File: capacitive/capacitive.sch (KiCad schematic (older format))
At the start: 53 parts, among them J101 I2C, J102 UART, J103 SWD, U101 STM32F070C6T6, U102 TLV9062IDR

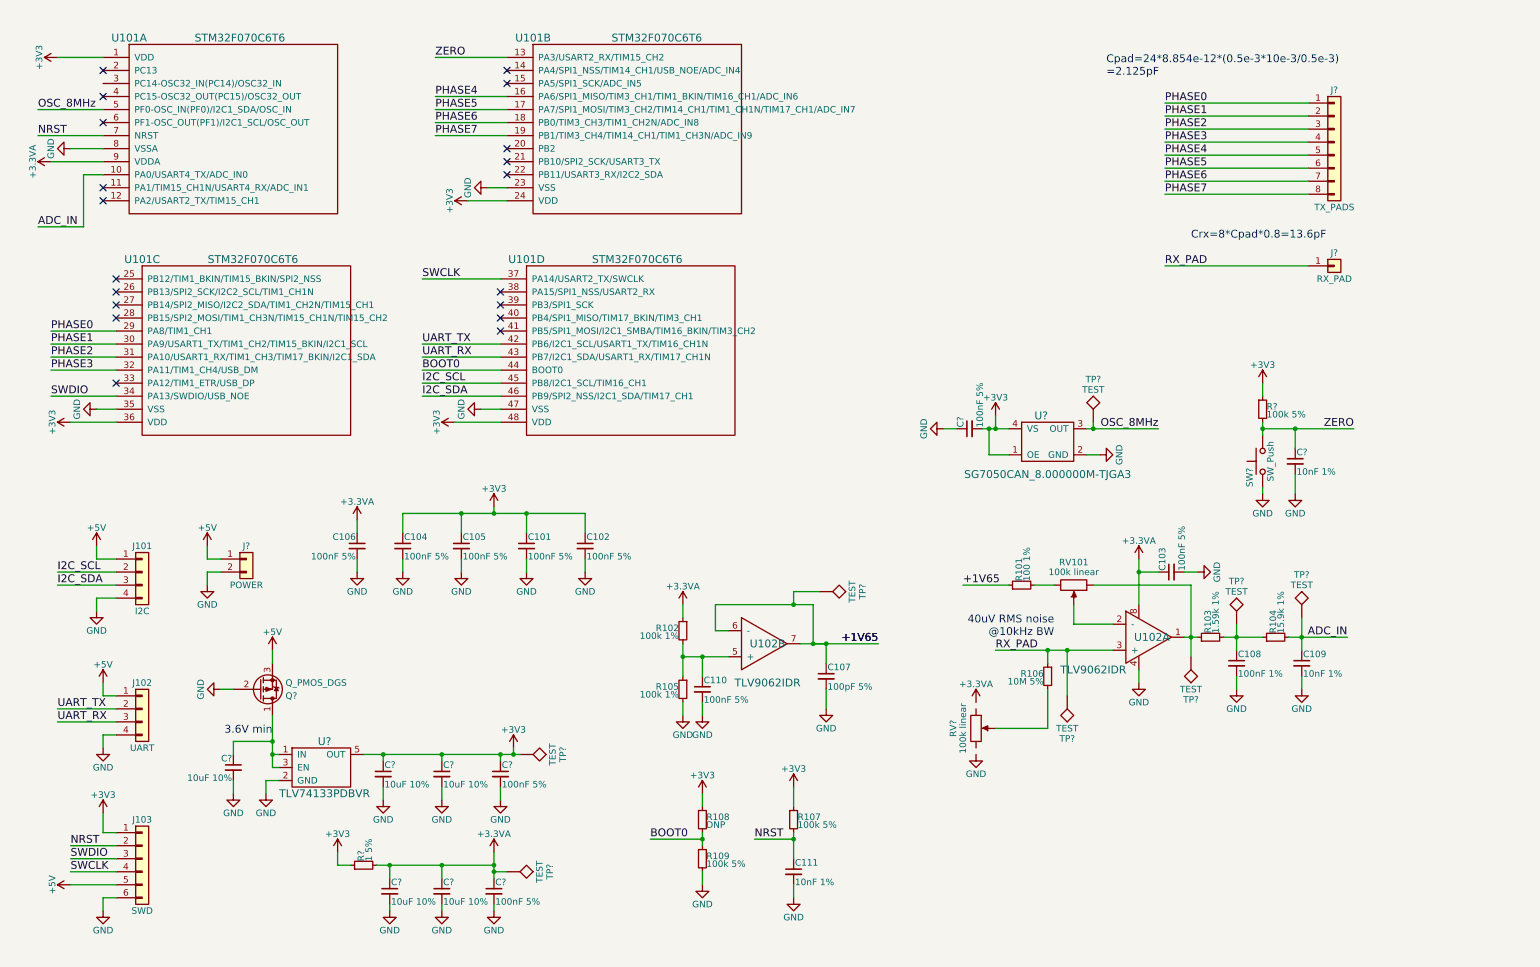
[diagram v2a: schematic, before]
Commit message: Write script to autofill components; save before test
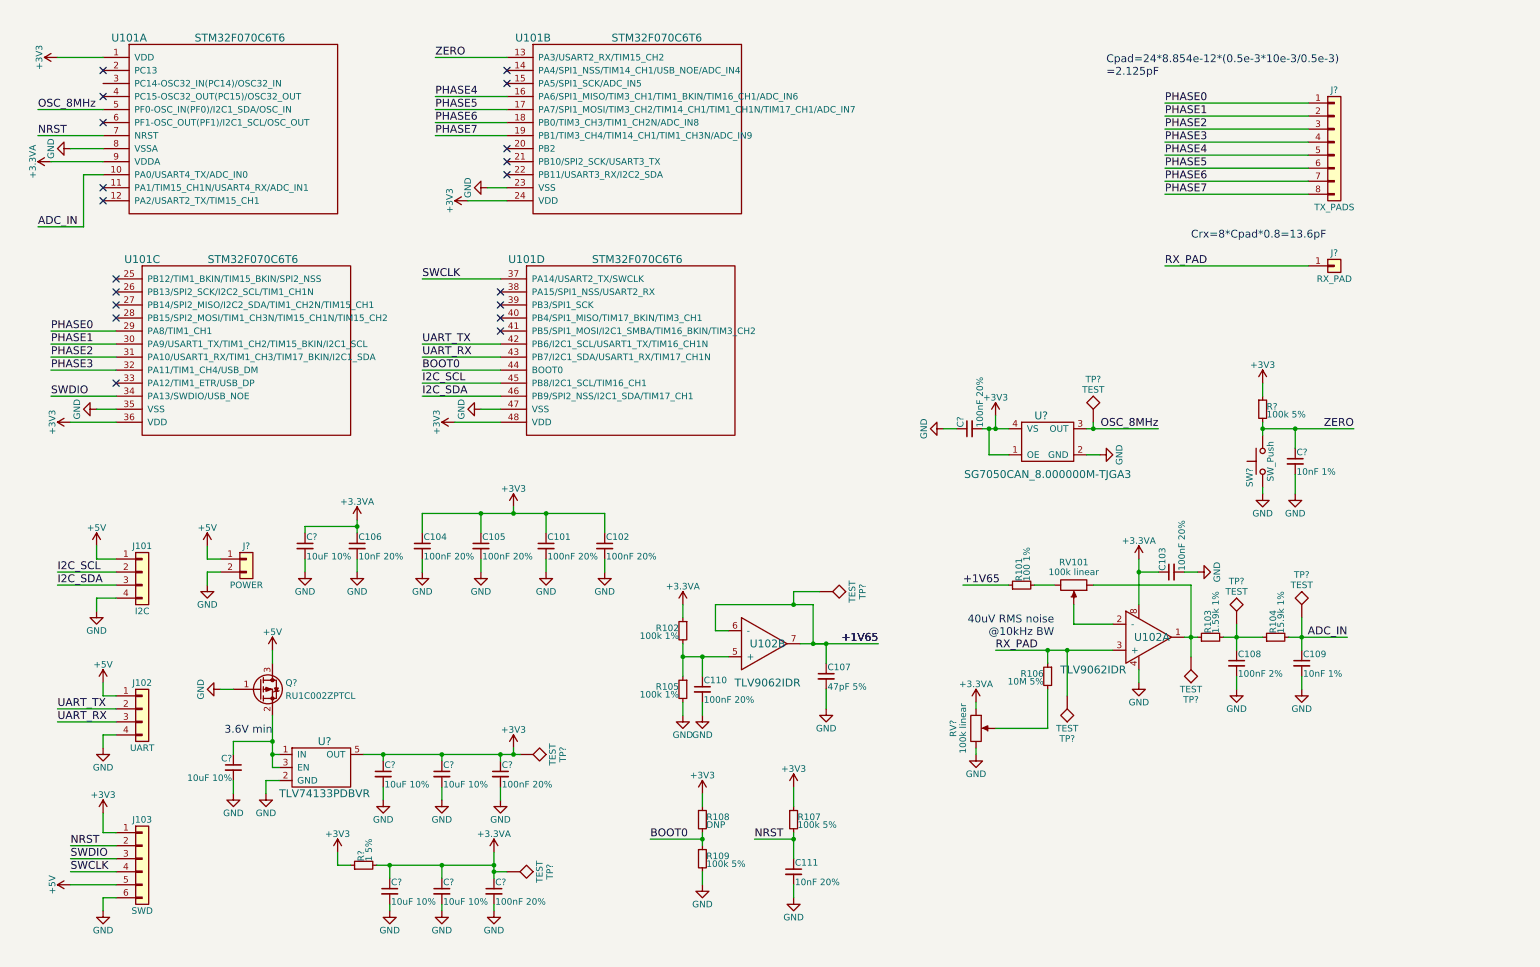
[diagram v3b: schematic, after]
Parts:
- removed Q?: Q_PMOS_DGS, symbol Q_PMOS_DGS
- added C?: 10uF 10%, Capacitors_SMD:C_1210_HandSoldering, symbol C_Small
- added Q?: RU1C002ZPTCL, symbol Q_PMOS_GSD
- C101, C102, C103, C105, C110, C? (x3): value 100nF 5% -> 100nF 20%
- C104: value 100nF 5% -> 100nF 20%; footprint (none) -> Capacitors_SMD:C_0805_HandSoldering; Mouser (none) -> 710-885012207016
- C106: value 100nF 5% -> 10nF 20%
- C107: value 100pF 5% -> 47pF 5%
- C108: value 100nF 1% -> 100nF 2%
- C111: value 10nF 1% -> 10nF 20%
- U101: Mouser (none) -> 511-STM32F070C6T6
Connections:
- net +3.3VA: now also RV?.1, C?.1
- net +5V: now also Q?.3 (D)
- net GND: now also RV?.3, C?.2, Q?.1 (G)
- net at C?.1, U?.1 (IN), U?.3 (EN): now also Q?.2 (S)
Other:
- moved on the sheet: C101, C102, C104, C105
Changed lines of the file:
@@
 L +3V3 #PWR110
 U 1 1 5AFFB346
-P 4250 4350
-F 0 "#PWR110" H 4250 4200 50  0001 C CNN
-F 1 "+3V3" H 4250 4490 50  0000 C CNN
-F 2 "" H 4250 4350 50  0001 C CNN
-F 3 "" H 4250 4350 50  0001 C CNN
-	1    4250 4350
+P 4400 4350
+F 0 "#PWR110" H 4400 4200 50  0001 C CNN
+F 1 "+3V3" H 4400 4490 50  0000 C CNN
+F 2 "" H 4400 4350 50  0001 C CNN
+F 3 "" H 4400 4350 50  0001 C CNN
+	1    4400 4350
 	1    0    0    -1
 $EndComp
@@
 P 6550 7150
 F 0 "C111" H 6560 7220 50  0000 L CNN
-F 1 "10nF 1%" H 6560 7070 50  0000 L CNN
+F 1 "10nF 20%" H 6560 7070 50  0000 L CNN
 F 2 "" H 6550 7150 50  0001 C CNN
 F 3 "" H 6550 7150 50  0001 C CNN
@@
 P 9950 5550
 F 0 "C108" H 9960 5620 50  0000 L CNN
-F 1 "100nF 1%" H 9960 5470 50  0000 L CNN
+F 1 "100nF 2%" H 9960 5470 50  0000 L CNN
 F 2 "" H 9950 5550 50  0001 C CNN
 F 3 "" H 9950 5550 50  0001 C CNN
@@
 P 9450 4850
 F 0 "C103" H 9460 4920 50  0000 L CNN
-F 1 "100nF 5%" H 9460 4770 50  0000 L CNN
+F 1 "100nF 20%" H 9460 4770 50  0000 L CNN
 F 2 "" H 9450 4850 50  0001 C CNN
 F 3 "" H 9450 4850 50  0001 C CNN
@@
 P 5850 5750
 F 0 "C110" H 5860 5820 50  0000 L CNN
-F 1 "100nF 5%" H 5860 5670 50  0000 L CNN
+F 1 "100nF 20%" H 5860 5670 50  0000 L CNN
 F 2 "" H 5850 5750 50  0001 C CNN
 F 3 "" H 5850 5750 50  0001 C CNN
@@
 P 6800 5650
 F 0 "C107" H 6810 5720 50  0000 L CNN
-F 1 "100pF 5%" H 6810 5570 50  0000 L CNN
+F 1 "47pF 5%" H 6810 5570 50  0000 L CNN
 F 2 "" H 6800 5650 50  0001 C CNN
 F 3 "" H 6800 5650 50  0001 C CNN
@@
 L C_Small C101
 U 1 1 5B0020A9
-P 4500 4650
-F 0 "C101" H 4510 4720 50  0000 L CNN
-F 1 "100nF 5%" H 4510 4570 50  0000 L CNN
-F 2 "" H 4500 4650 50  0001 C CNN
-F 3 "" H 4500 4650 50  0001 C CNN
-	1    4500 4650
+P 4650 4650
+F 0 "C101" H 4660 4720 50  0000 L CNN
+F 1 "100nF 20%" H 4660 4570 50  0000 L CNN
+F 2 "" H 4650 4650 50  0001 C CNN
+F 3 "" H 4650 4650 50  0001 C CNN
+	1    4650 4650
 	1    0    0    -1
 $EndComp
@@
 L GND #PWR114
 U 1 1 5B0020AC
-P 4500 4850
-F 0 "#PWR114" H 4500 4600 50  0001 C CNN
-F 1 "GND" H 4500 4700 50  0000 C CNN
-F 2 "" H 4500 4850 50  0001 C CNN
-F 3 "" H 4500 4850 50  0001 C CNN
-	1    4500 4850
+P 4650 4850
+F 0 "#PWR114" H 4650 4600 50  0001 C CNN
+F 1 "GND" H 4650 4700 50  0000 C CNN
+F 2 "" H 4650 4850 50  0001 C CNN
+F 3 "" H 4650 4850 50  0001 C CNN
+	1    4650 4850
 	1    0    0    -1
 $EndComp
@@
 L C_Small C104
 U 1 1 5B0020B2
-P 3550 4650
-F 0 "C104" H 3560 4720 50  0000 L CNN
-F 1 "100nF 5%" H 3560 4570 50  0000 L CNN
-F 2 "" H 3550 4650 50  0001 C CNN
-F 3 "" H 3550 4650 50  0001 C CNN
-	1    3550 4650
+P 3700 4650
+F 0 "C104" H 3710 4720 50  0000 L CNN
+F 1 "100nF 20%" H 3710 4570 50  0000 L CNN
+F 2 "Capacitors_SMD:C_0805_HandSoldering" H 3700 4650 50  0001 C CNN
+F 3 "" H 3700 4650 50  0001 C CNN
+F 4 "710-885012207016" H 3700 4650 60  0001 C CNN "Mouser"
+	1    3700 4650
 	1    0    0    -1
 $EndComp
@@
 L GND #PWR118
 U 1 1 5B0020B3
-P 4000 4850
-F 0 "#PWR118" H 4000 4600 50  0001 C CNN
-F 1 "GND" H 4000 4700 50  0000 C CNN
-F 2 "" H 4000 4850 50  0001 C CNN
-F 3 "" H 4000 4850 50  0001 C CNN
-	1    4000 4850
+P 4150 4850
+F 0 "#PWR118" H 4150 4600 50  0001 C CNN
+F 1 "GND" H 4150 4700 50  0000 C CNN
+F 2 "" H 4150 4850 50  0001 C CNN
+F 3 "" H 4150 4850 50  0001 C CNN
+	1    4150 4850
 	1    0    0    -1
 $EndComp
@@
 L GND #PWR117
 U 1 1 5B0020B4
-P 3550 4850
-F 0 "#PWR117" H 3550 4600 50  0001 C CNN
-F 1 "GND" H 3550 4700 50  0000 C CNN
-F 2 "" H 3550 4850 50  0001 C CNN
-F 3 "" H 3550 4850 50  0001 C CNN
-	1    3550 4850
+P 3700 4850
+F 0 "#PWR117" H 3700 4600 50  0001 C CNN
+F 1 "GND" H 3700 4700 50  0000 C CNN
+F 2 "" H 3700 4850 50  0001 C CNN
+F 3 "" H 3700 4850 50  0001 C CNN
+	1    3700 4850
 	1    0    0    -1
 $EndComp
@@
 L C_Small C105
 U 1 1 5B0020B1
-P 4000 4650
-F 0 "C105" H 4010 4720 50  0000 L CNN
-F 1 "100nF 5%" H 4010 4570 50  0000 L CNN
-F 2 "" H 4000 4650 50  0001 C CNN
-F 3 "" H 4000 4650 50  0001 C CNN
-	1    4000 4650
+P 4150 4650
+F 0 "C105" H 4160 4720 50  0000 L CNN
+F 1 "100nF 20%" H 4160 4570 50  0000 L CNN
+F 2 "" H 4150 4650 50  0001 C CNN
+F 3 "" H 4150 4650 50  0001 C CNN
+	1    4150 4650
 	1    0    0    -1
 $EndComp
@@
 P 3200 4650
 F 0 "C106" H 3210 4720 50  0000 L CNN
-F 1 "100nF 5%" H 3210 4570 50  0000 L CNN
+F 1 "10nF 20%" H 3210 4570 50  0000 L CNN
 F 2 "" H 3200 4650 50  0001 C CNN
 F 3 "" H 3200 4650 50  0001 C CNN
 	1    3200 4650
-	-1   0    0    -1
+	1    0    0    -1
 $EndComp
 $Comp
 L C_Small C102
 U 1 1 5B0020B0
-P 4950 4650
-F 0 "C102" H 4960 4720 50  0000 L CNN
-F 1 "100nF 5%" H 4960 4570 50  0000 L CNN
-F 2 "" H 4950 4650 50  0001 C CNN
-F 3 "" H 4950 4650 50  0001 C CNN
-	1    4950 4650
+P 5100 4650
+F 0 "C102" H 5110 4720 50  0000 L CNN
+F 1 "100nF 20%" H 5110 4570 50  0000 L CNN
+F 2 "" H 5100 4650 50  0001 C CNN
+F 3 "" H 5100 4650 50  0001 C CNN
+	1    5100 4650
 	1    0    0    -1
 $EndComp
@@
 L GND #PWR115
 U 1 1 5B0020B5
-P 4950 4850
-F 0 "#PWR115" H 4950 4600 50  0001 C CNN
-F 1 "GND" H 4950 4700 50  0000 C CNN
-F 2 "" H 4950 4850 50  0001 C CNN
-F 3 "" H 4950 4850 50  0001 C CNN
-	1    4950 4850
+P 5100 4850
+F 0 "#PWR115" H 5100 4600 50  0001 C CNN
+F 1 "GND" H 5100 4700 50  0000 C CNN
+F 2 "" H 5100 4850 50  0001 C CNN
+F 3 "" H 5100 4850 50  0001 C CNN
+	1    5100 4850
 	1    0    0    -1
 $EndComp
@@
 F 2 "" H 1550 2450 60  0001 C CNN
 F 3 "" H 1550 2450 60  0001 C CNN
+F 4 "511-STM32F070C6T6" H 1550 2450 60  0001 C CNN "Mouser"
 	3    1550 2450
 	1    0    0    -1
@@
 P 4300 6400
 F 0 "C?" H 4310 6470 50  0000 L CNN
-F 1 "100nF 5%" H 4310 6320 50  0000 L CNN
+F 1 "100nF 20%" H 4310 6320 50  0000 L CNN
 F 2 "" H 4300 6400 50  0001 C CNN
 F 3 "" H 4300 6400 50  0001 C CNN
@@
 P 4250 7300
 F 0 "C?" H 4260 7370 50  0000 L CNN
-F 1 "100nF 5%" H 4260 7220 50  0000 L CNN
+F 1 "100nF 20%" H 4260 7220 50  0000 L CNN
 F 2 "" H 4250 7300 50  0001 C CNN
 F 3 "" H 4250 7300 50  0001 C CNN
@@
 P 7900 3750
 F 0 "C?" H 7910 3820 50  0000 L CNN
-F 1 "100nF 5%" H 7910 3670 50  0000 L CNN
+F 1 "100nF 20%" H 7910 3670 50  0000 L CNN
 F 2 "" H 7900 3750 50  0001 C CNN
 F 3 "" H 7900 3750 50  0001 C CNN
@@
 	1    8850 3700
 	1    0    0    -1
-$EndComp
-$Comp
-L Q_PMOS_DGS Q?
-U 1 1 5B009335
-P 2450 5750
-F 0 "Q?" H 2650 5800 50  0000 L CNN
-F 1 "Q_PMOS_DGS" H 2650 5700 50  0000 L CNN
-F 2 "" H 2650 5850 50  0001 C CNN
-F 3 "" H 2450 5750 50  0001 C CNN
-	1    2450 5750
-	1    0    0    1
 $EndComp
 $Comp
@@
 	1000 3700 1350 3700
 Wire Wire Line
-	4950 4400 4950 4550
-Wire Wire Line
-	3550 4400 3550 4550
+	5100 4400 5100 4550
+Wire Wire Line
+	3700 4400 3700 4550
 Wire Wire Line
 	6250 6900 6550 6900
@@
 	3200 4750 3200 4850
 Wire Wire Line
-	3550 4750 3550 4850
-Wire Wire Line
-	4000 4750 4000 4850
-Wire Wire Line
-	4000 4400 4000 4550
-Wire Wire Line
-	4250 4400 4250 4350
-Connection ~ 4250 4400
-Wire Wire Line
-	4500 4400 4500 4550
+	3700 4750 3700 4850
+Wire Wire Line
+	4150 4750 4150 4850
+Wire Wire Line
+	4150 4400 4150 4550
+Wire Wire Line
+	4400 4400 4400 4350
+Connection ~ 4400 4400
+Wire Wire Line
+	4650 4400 4650 4550
 Wire Wire Line
 	3800 1300 4350 1300
@@
 	2500 6450 2600 6450
 Wire Wire Line
-	4500 4750 4500 4850
-Wire Wire Line
-	4950 4750 4950 4850
+	4650 4750 4650 4850
+Wire Wire Line
+	5100 4750 5100 4850
 Wire Wire Line
 	3250 6250 4450 6250
@@
 Connection ~ 3400 6250
 Wire Wire Line
-	3550 4400 4950 4400
-Connection ~ 4000 4400
-Connection ~ 4500 4400
+	3700 4400 5100 4400
+Connection ~ 4150 4400
+Connection ~ 4650 4400
 Wire Wire Line
 	3350 7100 4250 7100
@@
 Wire Wire Line
 	3050 7100 3150 7100
+$Comp
+L Q_PMOS_GSD Q?
+U 1 1 5B007344
+P 2450 5750
+F 0 "Q?" H 2650 5800 50  0000 L CNN
+F 1 "RU1C002ZPTCL" H 2650 5700 50  0000 L CNN
+F 2 "" H 2650 5850 50  0001 C CNN
+F 3 "" H 2450 5750 50  0001 C CNN
+F 4 "755-RU1C002ZPTCL" H 2450 5750 60  0001 C CNN "Mouser"
+	1    2450 5750
+	1    0    0    -1
+$EndComp
+Wire Wire Line
+	7950 6200 7950 6250
+Wire Wire Line
+	7950 5850 7950 5900
+$Comp
+L C_Small C?
+U 1 1 5B00A972
+P 2800 4650
+F 0 "C?" H 2810 4720 50  0000 L CNN
+F 1 "10uF 10%" H 2810 4570 50  0000 L CNN
+F 2 "Capacitors_SMD:C_1210_HandSoldering" H 2800 4650 50  0001 C CNN
+F 3 "" H 2800 4650 50  0001 C CNN
+F 4 "581-TAJB106K020RNJV" H 2800 4650 60  0001 C CNN "Mouser"
+	1    2800 4650
+	1    0    0    -1
+$EndComp
+$Comp
+L GND #PWR?
+U 1 1 5B00ACDE
+P 2800 4850
+F 0 "#PWR?" H 2800 4600 50  0001 C CNN
+F 1 "GND" H 2800 4700 50  0000 C CNN
+F 2 "" H 2800 4850 50  0001 C CNN
+F 3 "" H 2800 4850 50  0001 C CNN
+	1    2800 4850
+	1    0    0    -1
+$EndComp
+Wire Wire Line
+	2800 4850 2800 4750
+Wire Wire Line
+	2800 4550 2800 4500
+Wire Wire Line
+	2800 4500 3200 4500
+Connection ~ 3200 4500
 $EndSCHEMATC

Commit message: Autofill works!
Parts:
- C101, C102, C103, C105, C110, C? (x3): footprint (none) -> Capacitors_SMD:C_0805_HandSoldering; Mouser (none) -> 710-885012207016
- C? (x5): footprint (none) -> Capacitors_SMD:C_1210_HandSoldering; Mouser (none) -> 581-TAJB106K020RNJV
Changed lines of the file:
@@
 F 0 "C103" H 9460 4920 50  0000 L CNN
 F 1 "100nF 20%" H 9460 4770 50  0000 L CNN
-F 2 "" H 9450 4850 50  0001 C CNN
+F 2 "Capacitors_SMD:C_0805_HandSoldering" H 9450 4850 50  0001 C CNN
 F 3 "" H 9450 4850 50  0001 C CNN
+F 4 "710-885012207016" H 9450 4850 50  0001 C "Mouser"
 	1    9450 4850
 	0    -1   -1   0
@@
 F 0 "C110" H 5860 5820 50  0000 L CNN
 F 1 "100nF 20%" H 5860 5670 50  0000 L CNN
-F 2 "" H 5850 5750 50  0001 C CNN
+F 2 "Capacitors_SMD:C_0805_HandSoldering" H 5850 5750 50  0001 C CNN
 F 3 "" H 5850 5750 50  0001 C CNN
+F 4 "710-885012207016" H 5850 5750 50  0001 C "Mouser"
 	1    5850 5750
 	1    0    0    -1
@@
 F 0 "C101" H 4660 4720 50  0000 L CNN
 F 1 "100nF 20%" H 4660 4570 50  0000 L CNN
-F 2 "" H 4650 4650 50  0001 C CNN
+F 2 "Capacitors_SMD:C_0805_HandSoldering" H 4650 4650 50  0001 C CNN
 F 3 "" H 4650 4650 50  0001 C CNN
+F 4 "710-885012207016" H 4650 4650 50  0001 C "Mouser"
 	1    4650 4650
 	1    0    0    -1
@@
 F 0 "C105" H 4160 4720 50  0000 L CNN
 F 1 "100nF 20%" H 4160 4570 50  0000 L CNN
-F 2 "" H 4150 4650 50  0001 C CNN
+F 2 "Capacitors_SMD:C_0805_HandSoldering" H 4150 4650 50  0001 C CNN
 F 3 "" H 4150 4650 50  0001 C CNN
+F 4 "710-885012207016" H 4150 4650 50  0001 C "Mouser"
 	1    4150 4650
 	1    0    0    -1
@@
 F 0 "C102" H 5110 4720 50  0000 L CNN
 F 1 "100nF 20%" H 5110 4570 50  0000 L CNN
-F 2 "" H 5100 4650 50  0001 C CNN
+F 2 "Capacitors_SMD:C_0805_HandSoldering" H 5100 4650 50  0001 C CNN
 F 3 "" H 5100 4650 50  0001 C CNN
+F 4 "710-885012207016" H 5100 4650 50  0001 C "Mouser"
 	1    5100 4650
 	1    0    0    -1
@@
 F 0 "C?" H 4310 6470 50  0000 L CNN
 F 1 "100nF 20%" H 4310 6320 50  0000 L CNN
-F 2 "" H 4300 6400 50  0001 C CNN
+F 2 "Capacitors_SMD:C_0805_HandSoldering" H 4300 6400 50  0001 C CNN
 F 3 "" H 4300 6400 50  0001 C CNN
+F 4 "710-885012207016" H 4300 6400 50  0001 C "Mouser"
 	1    4300 6400
 	1    0    0    -1
@@
 F 0 "C?" H 3860 7370 50  0000 L CNN
 F 1 "10uF 10%" H 3860 7220 50  0000 L CNN
-F 2 "" H 3850 7300 50  0001 C CNN
+F 2 "Capacitors_SMD:C_1210_HandSoldering" H 3850 7300 50  0001 C CNN
 F 3 "" H 3850 7300 50  0001 C CNN
+F 4 "581-TAJB106K020RNJV" H 3850 7300 50  0001 C "Mouser"
 	1    3850 7300
 	1    0    0    -1
@@
 F 0 "C?" H 4260 7370 50  0000 L CNN
 F 1 "100nF 20%" H 4260 7220 50  0000 L CNN
-F 2 "" H 4250 7300 50  0001 C CNN
+F 2 "Capacitors_SMD:C_0805_HandSoldering" H 4250 7300 50  0001 C CNN
 F 3 "" H 4250 7300 50  0001 C CNN
+F 4 "710-885012207016" H 4250 7300 50  0001 C "Mouser"
 	1    4250 7300
 	1    0    0    -1
@@
 F 0 "C?" H 7910 3820 50  0000 L CNN
 F 1 "100nF 20%" H 7910 3670 50  0000 L CNN
-F 2 "" H 7900 3750 50  0001 C CNN
+F 2 "Capacitors_SMD:C_0805_HandSoldering" H 7900 3750 50  0001 C CNN
 F 3 "" H 7900 3750 50  0001 C CNN
+F 4 "710-885012207016" H 7900 3750 50  0001 C "Mouser"
 	1    7900 3750
 	0    -1   -1   0
@@
 F 0 "C?" H 3410 6470 50  0000 L CNN
 F 1 "10uF 10%" H 3410 6320 50  0000 L CNN
-F 2 "" H 3400 6400 50  0001 C CNN
+F 2 "Capacitors_SMD:C_1210_HandSoldering" H 3400 6400 50  0001 C CNN
 F 3 "" H 3400 6400 50  0001 C CNN
+F 4 "581-TAJB106K020RNJV" H 3400 6400 50  0001 C "Mouser"
 	1    3400 6400
 	1    0    0    -1
@@
 F 0 "C?" H 3860 6470 50  0000 L CNN
 F 1 "10uF 10%" H 3860 6320 50  0000 L CNN
-F 2 "" H 3850 6400 50  0001 C CNN
+F 2 "Capacitors_SMD:C_1210_HandSoldering" H 3850 6400 50  0001 C CNN
 F 3 "" H 3850 6400 50  0001 C CNN
+F 4 "581-TAJB106K020RNJV" H 3850 6400 50  0001 C "Mouser"
 	1    3850 6400
 	1    0    0    -1
@@
 F 0 "C?" H 3460 7370 50  0000 L CNN
 F 1 "10uF 10%" H 3460 7220 50  0000 L CNN
-F 2 "" H 3450 7300 50  0001 C CNN
+F 2 "Capacitors_SMD:C_1210_HandSoldering" H 3450 7300 50  0001 C CNN
 F 3 "" H 3450 7300 50  0001 C CNN
+F 4 "581-TAJB106K020RNJV" H 3450 7300 50  0001 C "Mouser"
 	1    3450 7300
 	1    0    0    -1
@@
 F 0 "C?" H 2260 6420 50  0000 L CNN
 F 1 "10uF 10%" H 2260 6270 50  0000 L CNN
-F 2 "" H 2250 6350 50  0001 C CNN
+F 2 "Capacitors_SMD:C_1210_HandSoldering" H 2250 6350 50  0001 C CNN
 F 3 "" H 2250 6350 50  0001 C CNN
+F 4 "581-TAJB106K020RNJV" H 2250 6350 50  0001 C "Mouser"
 	1    2250 6350
 	-1   0    0    -1
